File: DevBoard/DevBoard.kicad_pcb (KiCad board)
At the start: 4 copper layers, 50 x 50 mm, 43 parts, among them J1 12V, J2 USB C, U1 STM32F103T6Ux, U2 TPS54202DDC, U3 TLV75533PDBV

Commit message: Initial layout/schematic
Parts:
- added C13: 10p, Capacitor_SMD:C_0603_1608Metric_Pad1.08x0.95mm_HandSolder, F.Cu at (101.0, 79.9)
- added C14: 10p, Capacitor_SMD:C_0603_1608Metric_Pad1.08x0.95mm_HandSolder, F.Cu at (101.0, 82.4)
- added C15: 0.1u, Capacitor_SMD:C_0603_1608Metric_Pad1.08x0.95mm_HandSolder, F.Cu at (101.0, 84.9)
- added C16: 0.1u, Capacitor_SMD:C_0603_1608Metric_Pad1.08x0.95mm_HandSolder, F.Cu at (144.4, 102.2)
- added C17: 0.1u, Capacitor_SMD:C_0603_1608Metric_Pad1.08x0.95mm_HandSolder, F.Cu at (155.7, 103.5)
- added C18: 0.1u, Capacitor_SMD:C_0603_1608Metric_Pad1.08x0.95mm_HandSolder, F.Cu at (155.7, 102.0)
- added C19: 0.1u, Capacitor_SMD:C_0603_1608Metric_Pad1.08x0.95mm_HandSolder, F.Cu at (158.4, 96.8)
- added C20: 0.1u, Capacitor_SMD:C_0603_1608Metric_Pad1.08x0.95mm_HandSolder, F.Cu at (144.1, 93.6)
- added C21: 4.7u, Capacitor_SMD:C_0805_2012Metric_Pad1.18x1.45mm_HandSolder, F.Cu at (158.6, 95.0)
- added J3: JTAG/SWD, Connector_PinHeader_1.27mm:PinHeader_2x07_P1.27mm_Vertical_SMD, F.Cu at (132.4, 113.0)
- added J4: Conn_01x12, Connector_PinHeader_2.54mm:PinHeader_1x12_P2.54mm_Vertical, F.Cu at (171.0, 86.1)
- added R10: 1k, Resistor_SMD:R_0402_1005Metric_Pad0.72x0.64mm_HandSolder, F.Cu at (157.9, 98.0)
- added R11: 10k, Resistor_SMD:R_0603_1608Metric_Pad0.98x0.95mm_HandSolder, F.Cu at (101.0, 89.9)
- added R12: 10k, Resistor_SMD:R_0603_1608Metric_Pad0.98x0.95mm_HandSolder, F.Cu at (101.0, 92.4)
- added R13: 10k, Resistor_SMD:R_0603_1608Metric_Pad0.98x0.95mm_HandSolder, F.Cu at (101.0, 94.9)
- added R14: 10k, Resistor_SMD:R_0603_1608Metric_Pad0.98x0.95mm_HandSolder, F.Cu at (155.7, 105.2)
- added R15: 100k, Resistor_SMD:R_0603_1608Metric_Pad0.98x0.95mm_HandSolder, F.Cu at (59.8, 39.7)
- added R16: 10k, Resistor_SMD:R_0603_1608Metric_Pad0.98x0.95mm_HandSolder, F.Cu at (59.8, 42.2)
- added R17: 100, Resistor_SMD:R_0603_1608Metric_Pad0.98x0.95mm_HandSolder, F.Cu at (59.8, 44.7)
- added TP10: TestPoint, TestPoint:TestPoint_Pad_D2.0mm, F.Cu at (47.5, 35.1)
- added TP11: TestPoint, TestPoint:TestPoint_Pad_D2.0mm, F.Cu at (51.6, 27.0)
- added TP12: TestPoint, TestPoint:TestPoint_Pad_D2.0mm, F.Cu at (51.6, 31.1)
- added TP13: TestPoint, TestPoint:TestPoint_Pad_D2.0mm, F.Cu at (51.6, 35.1)
- added TP14: TestPoint, TestPoint:TestPoint_Pad_D2.0mm, F.Cu at (55.6, 27.0)
- added TP15: TestPoint, TestPoint:TestPoint_Pad_D2.0mm, F.Cu at (55.6, 31.1)
- added TP16: TestPoint, TestPoint:TestPoint_Pad_D2.0mm, F.Cu at (55.6, 35.1)
- added TP8: TestPoint, TestPoint:TestPoint_Pad_D2.0mm, F.Cu at (47.5, 27.0)
- added TP9: TestPoint, TestPoint:TestPoint_Pad_D2.0mm, F.Cu at (47.5, 31.1)
- added U4: ~, CustomKicadFootprints:SAM-M10Q, F.Cu at (150.0, 115.0)
- added Y1: 8MHz, Crystal:Crystal_SMD_Abracon_ABM8G-4Pin_3.2x2.5mm, F.Cu at (160.7, 99.7)
- U1: value STM32F103T6Ux -> STM32F103C6Tx; footprint Package_DFN_QFN:QFN-36-1EP_6x6mm_P0.5mm_EP4.1x4.1mm -> Package_QFP:LQFP-48_7x7mm_P0.5mm
- moved D2 2.96 mm to (138.4, 100.5)
- moved U1 2.00 mm to (150.0, 98.0), turned to 180 degrees
- moved U3 0.13 mm to (150.7, 79.1)
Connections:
- U1 pad 10: unconnected-(U1-PA3-Pad10) -> /GPS_INT
- U1 pad 11: unconnected-(U1-PA4-Pad11) -> /PA1
- U1 pad 12: unconnected-(U1-PA5-Pad12) -> /PA2
- U1 pad 15: unconnected-(U1-PB0-Pad15) -> /PA5
- U1 pad 16: unconnected-(U1-PB1-Pad16) -> /PA6
- U1 pad 17: unconnected-(U1-PB2-Pad17) -> /PA7
- U1 pad 18: GND -> unconnected-(U1-PB0-Pad18)
- U1 pad 19: +3V3 -> unconnected-(U1-PB1-Pad19)
- U1 pad 2: unconnected-(U1-PD0-Pad2) -> /PC13
- U1 pad 20: unconnected-(U1-PA8-Pad20) -> /BOOT1
- U1 pad 23: unconnected-(U1-PA11-Pad23) -> GND
- U1 pad 24: unconnected-(U1-PA12-Pad24) -> +3V3
- U1 pad 26: GND -> unconnected-(U1-PB13-Pad26)
- U1 pad 27: +3V3 -> unconnected-(U1-PB14-Pad27)
- U1 pad 3: unconnected-(U1-PD1-Pad3) -> /PC14
- U1 pad 30: unconnected-(U1-PB3-Pad30) -> /GPS_TX
- U1 pad 31: unconnected-(U1-PB4-Pad31) -> /GPS_RX
- U1 pad 32: unconnected-(U1-PB5-Pad32) -> /USB_DN
- U1 pad 33: unconnected-(U1-PB6-Pad33) -> /USB_DP
- U1 pad 34: unconnected-(U1-PB7-Pad34) -> /JTAG_TMS
- U1 pad 35: unconnected-(U1-BOOT0-Pad35) -> GND
- U1 pad 36: GND -> +3V3
- U1 pad 37: GND -> /JTAG_TCK
- U1 pad 4: unconnected-(U1-NRST-Pad4) -> /PC15
- U1 pad 5: GND -> Net-(U1-PD0)
- U1 pad 6: +3V3 -> Net-(U1-PD1)
- U1 pad 7: unconnected-(U1-PA0-Pad7) -> /NRST
- U1 pad 8: unconnected-(U1-PA1-Pad8) -> GND
- U1 pad 9: unconnected-(U1-PA2-Pad9) -> +3V3
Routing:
- net +3V3: track 0.00 -> 90.1 mm, vias 0 -> 9
- net /GPS_INT: track 0.00 -> 32.8 mm, vias 0 -> 2
- net /PA1: track 0.00 -> 29.0 mm
- net /PA5: track 0.00 -> 27.7 mm
- net /PA2: track 0.00 -> 27.4 mm
- net /PA6: track 0.00 -> 26.2 mm
- net /PC13: track 0.00 -> 26.0 mm, vias 0 -> 2
- net /PA7: track 0.00 -> 25.4 mm
- net /PC15: track 0.00 -> 25.3 mm, vias 0 -> 2
- net /PC14: track 0.00 -> 25.1 mm, vias 0 -> 2
- net /JTAG_NRST: track 0.00 -> 24.9 mm
- net /JTAG_TDO: track 0.00 -> 23.3 mm
- net /JTAG_TDI: track 0.00 -> 23.1 mm, vias 0 -> 2
- net /JTAG_TMS: track 0.00 -> 22.3 mm
- net /JTAG_TCK: track 0.00 -> 21.9 mm
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- added copper zone on F.Cu, net +3V3
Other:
- board text added: "STM32F103 Rev A0.1 MD"
- board text removed: "STM32F103 Dev Board Rev A0.1 MD"

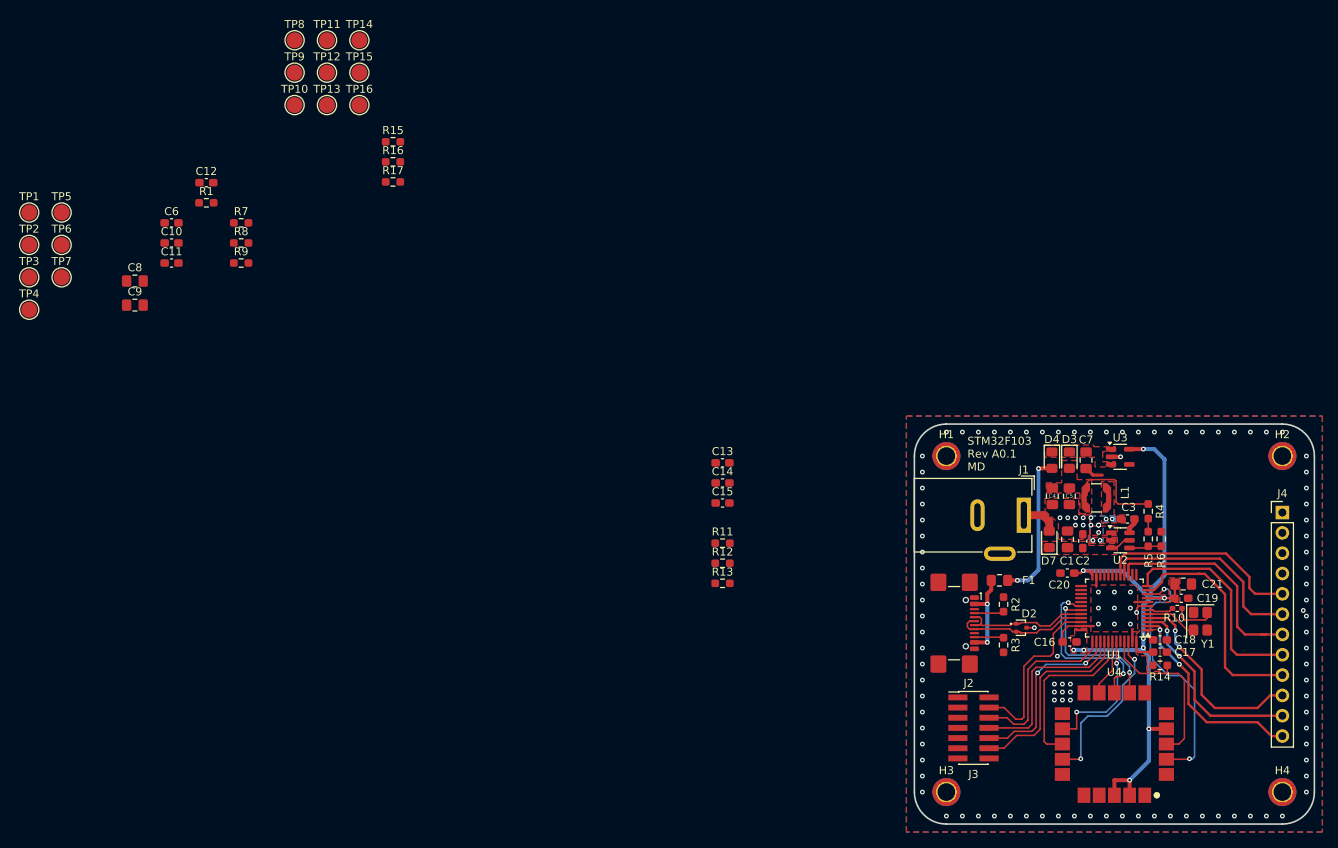
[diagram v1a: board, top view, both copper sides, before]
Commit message: Updates to DRC/schematic/layout. Layout to be redone.
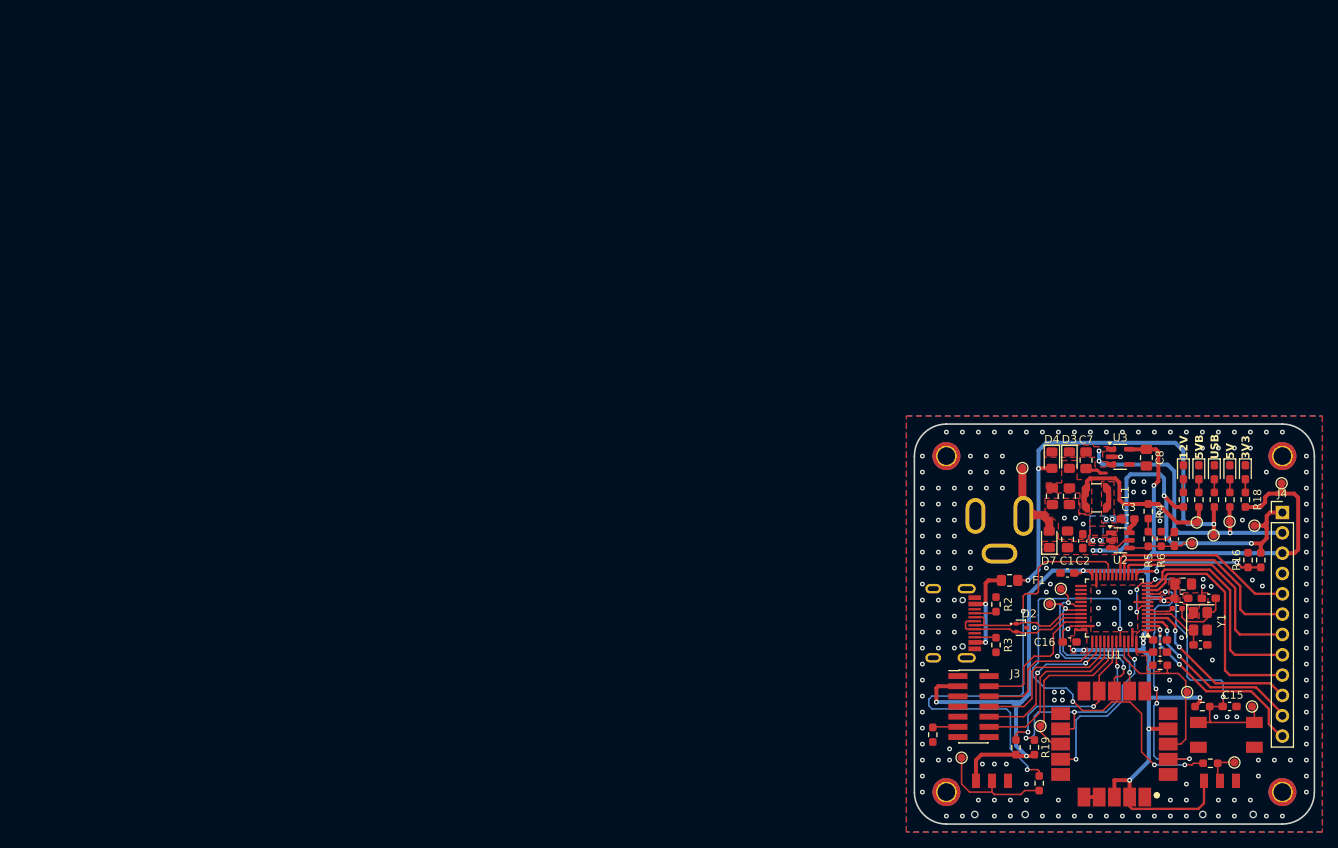
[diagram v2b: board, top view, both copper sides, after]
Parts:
- removed C10, C11, C12: 0.1u, Capacitor_SMD:C_0603_1608Metric_Pad1.08x0.95mm_HandSolder
- removed C9: 10U, Capacitor_SMD:C_0805_2012Metric_Pad1.18x1.45mm_HandSolder
- removed J2: USB C, Connector_USB:USB_C_Receptacle_GCT_USB4110
- removed TP14, TP15: TestPoint, TestPoint:TestPoint_Pad_D2.0mm
- added D1: RED, LED_SMD:LED_0603_1608Metric_Pad1.05x0.95mm_HandSolder, F.Cu at (158.6, 81.0)
- added D10: BLUE, LED_SMD:LED_0603_1608Metric_Pad1.05x0.95mm_HandSolder, F.Cu at (166.4, 81.0)
- added D5: RED, LED_SMD:LED_0603_1608Metric_Pad1.05x0.95mm_HandSolder, F.Cu at (160.6, 81.0)
- added D6: BLUE, LED_SMD:LED_0603_1608Metric_Pad1.05x0.95mm_HandSolder, F.Cu at (162.5, 81.0)
- added D9: BLUE, LED_SMD:LED_0603_1608Metric_Pad1.05x0.95mm_HandSolder, F.Cu at (164.4, 81.0)
- added J5: PRT-00119, CustomKicadFootprints:BarrelJack_3Pin_PJ202A, F.Cu at (135.6, 86.5)
- added R18: 1k, Resistor_SMD:R_0603_1608Metric_Pad0.98x0.95mm_HandSolder, F.Cu at (166.4, 84.5)
- added R19: 4.7k, Resistor_SMD:R_0603_1608Metric_Pad0.98x0.95mm_HandSolder, F.Cu at (140.0, 115.4)
- added R20: 4.7k, Resistor_SMD:R_0603_1608Metric_Pad0.98x0.95mm_HandSolder, F.Cu at (137.7, 115.4)
- added SW2: SLW-88229-2-SMT-TR, CustomKicadFootprints:SLW-88229-2-SMT-TR, F.Cu at (134.7, 121.4)
- added SW4: SLW-88229-2-SMT-TR, CustomKicadFootprints:SLW-88229-2-SMT-TR, F.Cu at (163.2, 121.4)
- added U5: TE 1571563-6, CustomKicadFootprints:506-1571563-6, F.Cu at (164.0, 113.8)
- J1: value 12V -> UJ20-C-H-G-SMT-2A-P16-TR; footprint Connector_BarrelJack:BarrelJack_Wuerth_6941xx301002 -> CustomKicadFootprints:UJ20-C-H-G-SMT-2A-P16-TR
- TP1, TP10, TP11, TP12, TP13, TP16, TP2, TP3, TP4, TP5, TP6, TP7, TP8, TP9: footprint TestPoint:TestPoint_Pad_D2.0mm -> TestPoint:TestPoint_Pad_D1.0mm
- U1: value STM32F103C6Tx -> STM32F103C6T7A
- moved TP2 157.1 mm to (167.5, 87.7)
- moved TP6 155.4 mm to (170.9, 82.4)
- moved TP5 151.0 mm to (164.4, 87.2)
- moved TP3 149.1 mm to (160.3, 87.3)
- moved TP4 148.3 mm to (159.7, 89.9)
- moved TP7 147.6 mm to (162.4, 88.9)
- moved TP9 145.7 mm to (165.0, 117.3)
- moved TP10 141.3 mm to (167.2, 110.3)
- moved C6 131.4 mm to (157.5, 89.4), turned to 90 degrees
- moved TP13 130.2 mm to (159.1, 108.5)
- moved C8 128.3 mm to (154.0, 79.2), turned to -90 degrees
- moved TP1 128.2 mm to (138.5, 80.5)
- moved R1 127.6 mm to (158.6, 84.5), turned to 90 degrees
- moved R9 127.1 mm to (164.4, 84.5), turned to 90 degrees
- moved R8 125.8 mm to (162.5, 84.5), turned to 90 degrees
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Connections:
- R2 pad 1: Net-(J2-CC1) -> Net-(J1-CC1)
- R3 pad 1: Net-(J2-CC2) -> Net-(J1-CC2)
- U1 pad 13: unconnected-(U1-PA3-Pad13) -> /aIN_12V_READ
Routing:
- net +3V3: track 90.1 -> 203.1 mm, vias 9 -> 12
- net /BOOT1: track 0.00 -> 61.6 mm, vias 0 -> 2
- net /BOOT0: track 0.00 -> 55.4 mm, vias 0 -> 4
- net +12V_D: track 2.67 -> 52.4 mm, vias 0 -> 4
- net /NRST: track 2.01 -> 43.8 mm, vias 1 -> 4
- net VBUS: track 18.7 -> 54.6 mm, vias 2 -> 3
- net +5V: track 0.00 -> 35.2 mm, vias 0 -> 3
- net /aIN_12V_READ: track 0.00 -> 16.7 mm, vias 0 -> 2
- net /SCL: track 7.12 -> 22.4 mm, vias 0 -> 2
- net Net-(SW2-B): track 0.00 -> 15.1 mm
- net /SDA: track 17.0 -> 26.5 mm, vias 2 -> 3
- net +5V_BOOST: track 12.7 -> 21.7 mm
- net +12V: track 4.70 -> 11.2 mm
- net /JTAG_TMS: track 22.3 -> 17.5 mm
- net Net-(C6-Pad2): track 1.70 -> 5.62 mm
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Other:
- board text added: "12V"
- board text added: "3V3"
- board text added: "5V"
- board text added: "5VB"
- board text added: "USB"

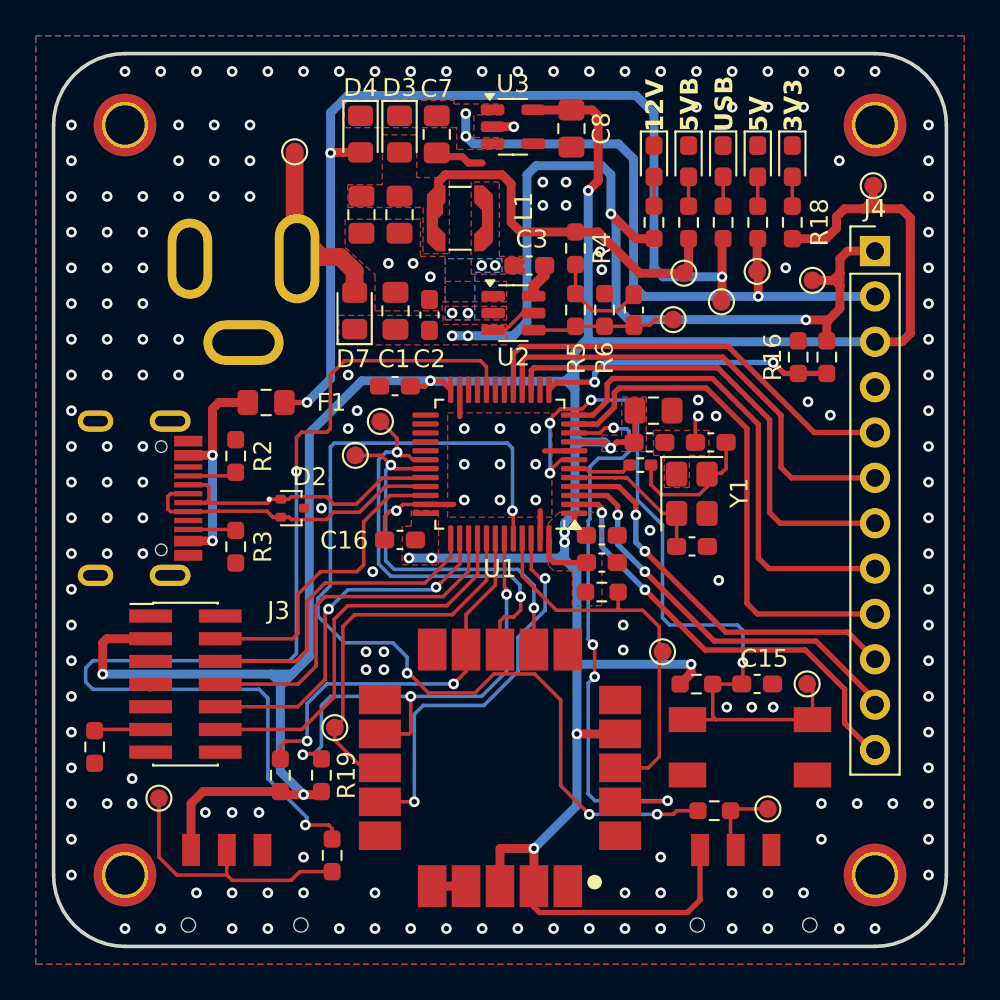
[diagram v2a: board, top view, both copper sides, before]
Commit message: A0.1 layout (not happy, will be redone again)
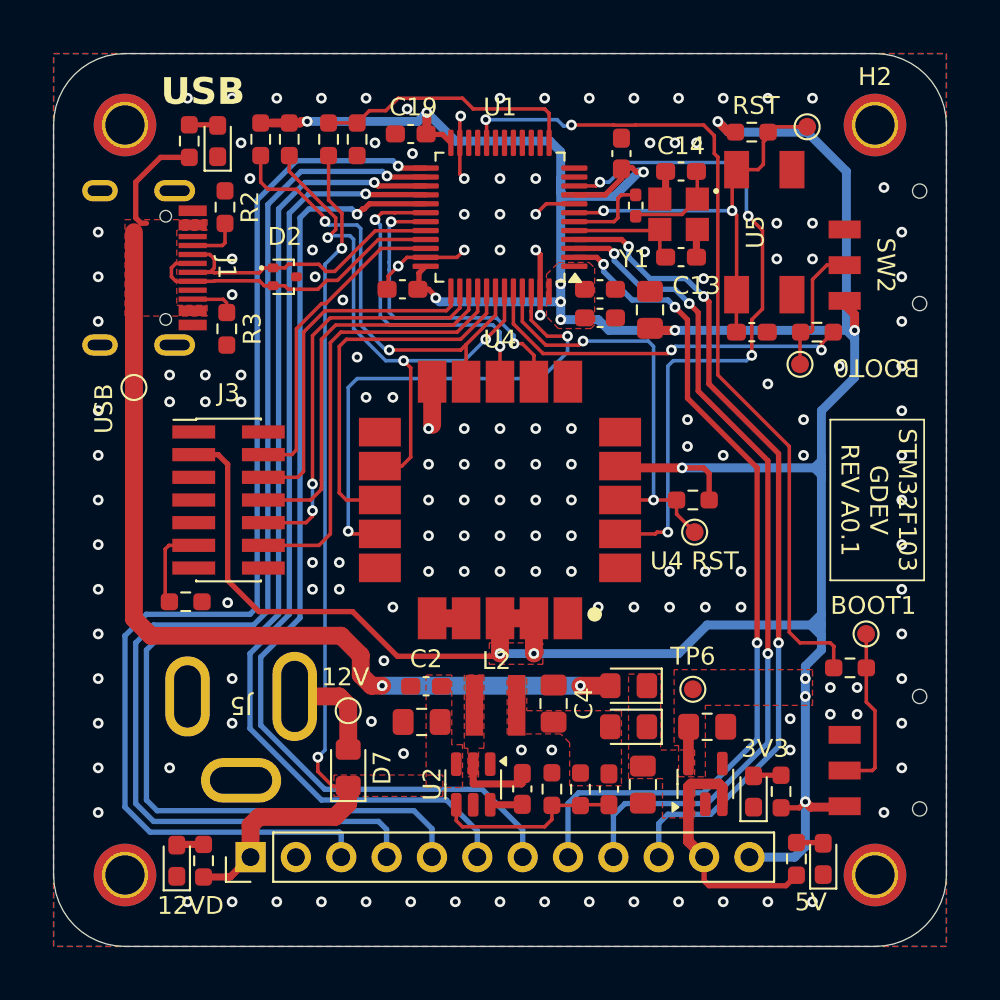
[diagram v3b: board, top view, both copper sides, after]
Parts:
- removed C5: 22u, Capacitor_SMD:C_0805_2012Metric_Pad1.18x1.45mm_HandSolder
- removed D5: RED, LED_SMD:LED_0603_1608Metric_Pad1.05x0.95mm_HandSolder
- removed F1: 1A, Fuse:Fuse_0805_2012Metric_Pad1.15x1.40mm_HandSolder
- removed L1: 15uH, Inductor_SMD:L_Coilcraft_LPS3314
- removed R4: 49.9, Resistor_SMD:R_0603_1608Metric_Pad0.98x0.95mm_HandSolder
- removed R7: 1k, Resistor_SMD:R_0603_1608Metric_Pad0.98x0.95mm_HandSolder
- removed TP11, TP12, TP16, TP2, TP3, TP4, TP5: TestPoint, TestPoint:TestPoint_Pad_D1.0mm
- added L2: 15u, CustomKicadFootprints:L_Coilcraft_XAL40, F.Cu at (149.8, 111.5)
- C4: value 22u -> 47u
- Y1: footprint Crystal:Crystal_SMD_Abracon_ABM8G-4Pin_3.2x2.5mm -> CustomKicadFootprints:Crystal_FC3BA
- moved SW2 50.2 mm to (171.1, 86.8), turned to -90 degrees
- moved J4 48.7 mm to (136.0, 120.0), turned to 90 degrees
- moved D1 47.4 mm to (131.9, 120.2), turned to 90 degrees
- moved R1 43.7 mm to (133.4, 120.2)
- moved TP8 43.4 mm to (166.8, 92.4)
- moved R12 39.9 mm to (167.8, 90.6), turned to 0 degrees
- moved D9 39.2 mm to (168.1, 120.1), turned to 90 degrees
- moved U3 38.3 mm to (161.5, 115.9), turned to 90 degrees
- moved C7 38.2 mm to (158.0, 115.9)
- moved R9 35.7 mm to (166.6, 120.1)
- moved R19 35.7 mm to (138.2, 79.8), turned to -90 degrees
- moved R20 35.6 mm to (136.6, 79.8), turned to -90 degrees
- moved D3 35.6 mm to (157.2, 112.7), turned to 180 degrees
- moved D10 35.4 mm to (164.2, 116.3), turned to 90 degrees
- moved C8 34.4 mm to (161.6, 112.7), turned to 0 degrees
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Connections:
- C6 pad 2: Net-(C6-Pad2) -> +5V_BOOST
- J1 pad A4: Net-(F1-Pad1) -> VBUS
- J1 pad A9: Net-(F1-Pad1) -> VBUS
- J1 pad B4: Net-(F1-Pad1) -> VBUS
- J1 pad B9: Net-(F1-Pad1) -> VBUS
- J4 pad 11: /PC14 -> +5V
- J4 pad 12: /PC13 -> +3V3
- J4 pad 2: +5V -> GND
- J4 pad 3: +3V3 -> /PB12
- J4 pad 4: GND -> /PB13
- J4 pad 5: /PA7 -> /PB14
- J4 pad 6: /PA6 -> /PB15
- J4 pad 7: /PA5 -> /PA8
- J4 pad 8: /PA2 -> /PC13
- J4 pad 9: /PA1 -> /PC14
- R11 pad 2: /BOOT0 -> /BOOT1
- R12 pad 2: /BOOT1 -> /BOOT0
- R5 pad 1: Net-(C6-Pad2) -> +5V_BOOST
- U1 pad 11: /PA1 -> unconnected-(U1-PA1-Pad11)
- U1 pad 12: /PA2 -> unconnected-(U1-PA2-Pad12)
- U1 pad 15: /PA5 -> unconnected-(U1-PA5-Pad15)
- U1 pad 16: /PA6 -> unconnected-(U1-PA6-Pad16)
- U1 pad 17: /PA7 -> unconnected-(U1-PA7-Pad17)
- U1 pad 25: unconnected-(U1-PB12-Pad25) -> /PB12
- U1 pad 26: unconnected-(U1-PB13-Pad26) -> /PB13
- U1 pad 27: unconnected-(U1-PB14-Pad27) -> /PB14
- U1 pad 28: unconnected-(U1-PB15-Pad28) -> /PB15
- U1 pad 29: unconnected-(U1-PA8-Pad29) -> /PA8
- U2 pad 5: +12V_D -> unconnected-(U2-EN-Pad5)
- Y1 pad 1: GND -> Net-(C14-Pad2)
- Y1 pad 2: Net-(U1-PD0) -> GND
- Y1 pad 3: GND -> Net-(U1-PD0)
- Y1 pad 4: Net-(C14-Pad2) -> GND
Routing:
- net /PB14: track 0.00 -> 66.5 mm, vias 0 -> 1
- net /PB13: track 0.00 -> 65.8 mm, vias 0 -> 1
- net /PB12: track 0.00 -> 65.0 mm, vias 0 -> 1
- net /PA8: track 0.00 -> 55.6 mm, vias 0 -> 1
- net /PB15: track 0.00 -> 54.4 mm, vias 0 -> 1
- net /BOOT0: track 55.4 -> 21.3 mm, vias 4 -> 2
- net /PA1: track 29.1 -> 0.00 mm
- net /PA5: track 27.1 -> 0.00 mm
- net /PA2: track 27.0 -> 0.00 mm
- net /PA6: track 26.0 -> 0.00 mm
- net /PA7: track 24.4 -> 0.00 mm
- net /PC15: track 22.1 -> 46.2 mm, vias 2 -> 3
- net /PC14: track 22.9 -> 47.1 mm, vias 2 -> 3
- net /PC13: track 24.7 -> 48.2 mm, vias 2 -> 3
- net +5V_BOOST: track 21.7 -> 0.00 mm
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- added copper zone on F.Cu, net VBUS
- removed copper zone on B.Cu, net Net-(U2-SW)
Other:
- board text added: "12VD"
- board text added: "BOOT0"
- board text added: "BOOT1"
- board text added: "RST"
- board text added: "STM32F103 GDEV REV A0.1"
- board text added: "U4 RST"
- board text removed: "5VB"
- board text removed: "STM32F103 Rev A0.1 MD"
